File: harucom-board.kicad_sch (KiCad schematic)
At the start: 4 parts

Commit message: Rev.2 (260322)
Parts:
- H1, H2, H3, H4: footprint MountingHole:MountingHole_2.2mm_M2_ISO14580 -> MountingHole:MountingHole_2.7mm_M2.5_Pad_Via; symbol Mechanical:MountingHole -> Mechanical:MountingHole_Pad
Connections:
- new net GND: H1.1, H2.1, H3.1, H4.1
- no-connect marks 1 -> 0
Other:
- sheet Connectors ports: added I2C0_SCL, I2C0_SDA, I2C1_SCL, I2C1_SDA; removed I2C_SDA, I2C_SDL, UART1_RX, UART1_TX
- sheet USB & Power Supply ports: added LED_G, LED_R; removed LED

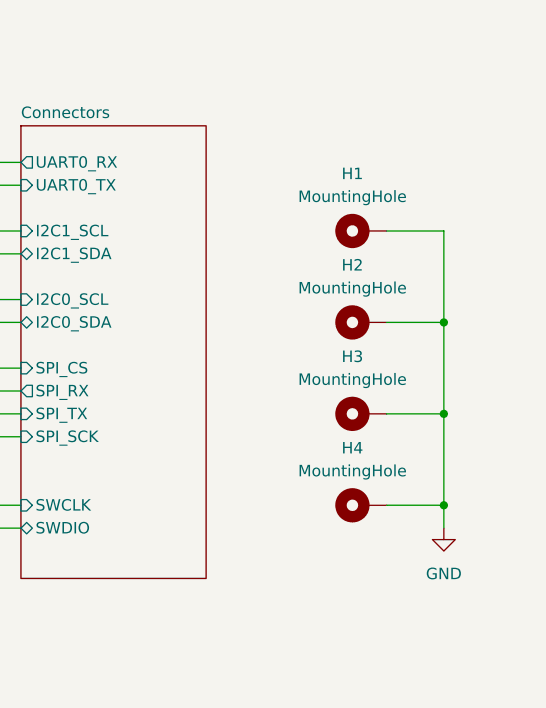
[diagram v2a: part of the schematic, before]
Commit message: Rev. 3B: Disconnect mounting holes from GND
  - Change mounting holes from MountingHole_Pad (with via) to MountingHole (ISO14580)
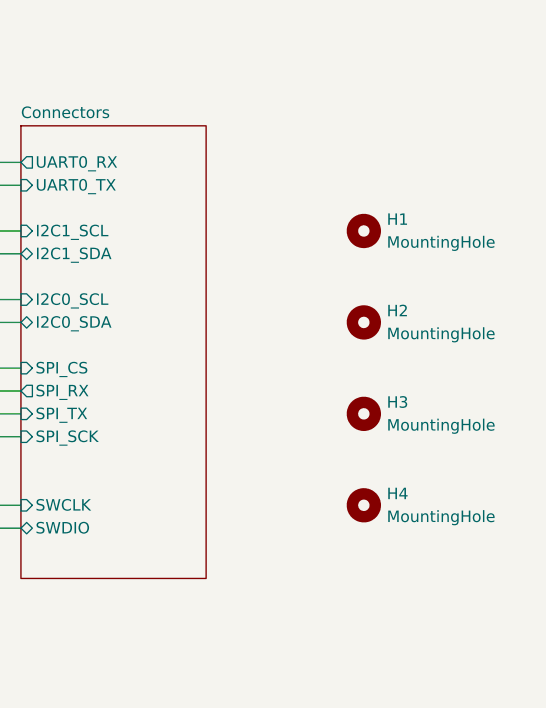
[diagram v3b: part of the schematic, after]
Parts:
- H1, H2, H3, H4: footprint MountingHole:MountingHole_2.7mm_M2.5_Pad_Via -> MountingHole:MountingHole_2.7mm_M2.5_ISO14580; symbol Mechanical:MountingHole_Pad -> Mechanical:MountingHole
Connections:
- removed net GND: H1.1, H2.1, H3.1, H4.1
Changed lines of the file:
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@@
 	(title_block
 		(title "Harucom-board")
-		(date "2026-03-23")
-		(rev "2B")
+		(date "2026-04-03")
+		(rev "3B")
 		(comment 1 "https://github.com/harukasan/harucom-board/")
 		(comment 2 "SPDX-License-Identifier: CERN-OHL-P-2.0")
@@
 		)
 	)
-	(junction
-		(at 240.03 143.51)
-		(diameter 0)
-		(color 0 0 0 0)
-	)
-	(junction
-		(at 240.03 133.35)
-		(diameter 0)
-		(color 0 0 0 0)
-	)
-	(junction
-		(at 240.03 123.19)
-		(diameter 0)
-		(color 0 0 0 0)
-	)
 	(wire
 		(pts
@@
 	(wire
 		(pts
-			(xy 240.03 143.51) (xy 240.03 133.35)
-		)
-		(stroke
-			(width 0)
-			(type default)
-		)
-	)
-	(wire
-		(pts
 			(xy 177.8 107.95) (xy 193.04 107.95)
 		)
@@
 	(wire
 		(pts
-			(xy 240.03 133.35) (xy 240.03 123.19)
-		)
-		(stroke
-			(width 0)
-			(type default)
-		)
-	)
-	(wire
-		(pts
 			(xy 78.74 63.5) (xy 91.44 63.5)
 		)
@@
 	(wire
 		(pts
-			(xy 240.03 123.19) (xy 233.68 123.19)
-		)
-		(stroke
-			(width 0)
-			(type default)
-		)
-	)
-	(wire
-		(pts
 			(xy 91.44 132.08) (xy 91.44 149.86)
 		)
@@
 	(wire
 		(pts
-			(xy 233.68 113.03) (xy 240.03 113.03)
-		)
-		(stroke
-			(width 0)
-			(type default)
-		)
-	)
-	(wire
-		(pts
-			(xy 240.03 143.51) (xy 233.68 143.51)
-		)
-		(stroke
-			(width 0)
-			(type default)
-		)
-	)
-	(wire
-		(pts
 			(xy 177.8 123.19) (xy 193.04 123.19)
 		)
@@
 	(wire
 		(pts
-			(xy 240.03 113.03) (xy 240.03 123.19)
-		)
-		(stroke
-			(width 0)
-			(type default)
-		)
-	)
-	(wire
-		(pts
 			(xy 177.8 133.35) (xy 193.04 133.35)
 		)
@@
 	(wire
 		(pts
-			(xy 240.03 133.35) (xy 233.68 133.35)
-		)
-		(stroke
-			(width 0)
-			(type default)
-		)
-	)
-	(wire
-		(pts
 			(xy 121.92 66.04) (xy 104.14 66.04)
 		)
@@
 	(wire
 		(pts
-			(xy 240.03 146.05) (xy 240.03 143.51)
-		)
-		(stroke
-			(width 0)
-			(type default)
-		)
-	)
-	(wire
-		(pts
 			(xy 53.34 87.63) (xy 71.12 87.63)
 		)
@@
 	)
 	(symbol
-		(lib_id "Mechanical:MountingHole_Pad")
+		(lib_id "Mechanical:MountingHole")
 		(at 231.14 133.35 90)
 		(unit 1)
@@
 		(fields_autoplaced yes)
 		(property "Reference" "H3"
-			(at 229.87 127 90)
+			(at 233.68 132.0799 90)
 			(effects
 				(font
 					(size 1.27 1.27)
 				)
+				(justify right)
 			)
 		)
 		(property "Value" "MountingHole"
-			(at 229.87 129.54 90)
+			(at 233.68 134.6199 90)
 			(effects
 				(font
 					(size 1.27 1.27)
 				)
+				(justify right)
 			)
 		)
-		(property "Footprint" "MountingHole:MountingHole_2.7mm_M2.5_Pad_Via"
+		(property "Footprint" "MountingHole:MountingHole_2.7mm_M2.5_ISO14580"
 			(at 231.14 133.35 0)
 			(effects
@@
 			)
 		)
-		(property "Description" "Mounting Hole with connection"
+		(property "Description" "Mounting Hole without connection"
 			(at 231.14 133.35 0)
 			(effects
@@
 			)
 		)
-		(pin "1"
-		)
 		(instances
-			(project ""
+			(project "harucom-board"
 				(path "/0cb5192e-ac62-478f-bacb-beb1b9be1a5b"
 					(reference "H3")
@@
 	)
 	(symbol
-		(lib_id "Mechanical:MountingHole_Pad")
+		(lib_id "Mechanical:MountingHole")
 		(at 231.14 123.19 90)
 		(unit 1)
@@
 		(fields_autoplaced yes)
 		(property "Reference" "H2"
-			(at 229.87 116.84 90)
+			(at 233.68 121.9199 90)
 			(effects
 				(font
 					(size 1.27 1.27)
 				)
+				(justify right)
 			)
 		)
 		(property "Value" "MountingHole"
-			(at 229.87 119.38 90)
+			(at 233.68 124.4599 90)
 			(effects
 				(font
 					(size 1.27 1.27)
 				)
+				(justify right)
 			)
 		)
-		(property "Footprint" "MountingHole:MountingHole_2.7mm_M2.5_Pad_Via"
+		(property "Footprint" "MountingHole:MountingHole_2.7mm_M2.5_ISO14580"
 			(at 231.14 123.19 0)
 			(effects
@@
 			)
 		)
-		(property "Description" "Mounting Hole with connection"
+		(property "Description" "Mounting Hole without connection"
 			(at 231.14 123.19 0)
 			(effects
@@
 			)
 		)
-		(pin "1"
-		)
 		(instances
-			(project ""
+			(project "harucom-board"
 				(path "/0cb5192e-ac62-478f-bacb-beb1b9be1a5b"
 					(reference "H2")
@@
 	)
 	(symbol
-		(lib_id "Mechanical:MountingHole_Pad")
+		(lib_id "Mechanical:MountingHole")
 		(at 231.14 113.03 90)
 		(unit 1)
@@
 		(fields_autoplaced yes)
 		(property "Reference" "H1"
-			(at 229.87 106.68 90)
+			(at 233.68 111.7599 90)
 			(effects
 				(font
 					(size 1.27 1.27)
 				)
+				(justify right)
 			)
 		)
 		(property "Value" "MountingHole"
-			(at 229.87 109.22 90)
+			(at 233.68 114.2999 90)
 			(effects
 				(font
 					(size 1.27 1.27)
 				)
+				(justify right)
 			)
 		)
-		(property "Footprint" "MountingHole:MountingHole_2.7mm_M2.5_Pad_Via"
+		(property "Footprint" "MountingHole:MountingHole_2.7mm_M2.5_ISO14580"
 			(at 231.14 113.03 0)
 			(effects
@@
 			)
 		)
-		(property "Description" "Mounting Hole with connection"
+		(property "Description" "Mounting Hole without connection"
 			(at 231.14 113.03 0)
 			(effects
@@
 			)
 		)
-		(pin "1"
-		)
 		(instances
-			(project ""
+			(project "harucom-board"
 				(path "/0cb5192e-ac62-478f-bacb-beb1b9be1a5b"
 					(reference "H1")
@@
 	)
 	(symbol
-		(lib_id "Mechanical:MountingHole_Pad")
+		(lib_id "Mechanical:MountingHole")
 		(at 231.14 143.51 90)
 		(unit 1)
@@
 		(fields_autoplaced yes)
 		(property "Reference" "H4"
-			(at 229.87 137.16 90)
+			(at 233.68 142.2399 90)
 			(effects
 				(font
 					(size 1.27 1.27)
 				)
+				(justify right)
 			)
 		)
 		(property "Value" "MountingHole"
-			(at 229.87 139.7 90)
+			(at 233.68 144.7799 90)
 			(effects
 				(font
 					(size 1.27 1.27)
 				)
+				(justify right)
 			)
 		)
-		(property "Footprint" "MountingHole:MountingHole_2.7mm_M2.5_Pad_Via"
+		(property "Footprint" "MountingHole:MountingHole_2.7mm_M2.5_ISO14580"
 			(at 231.14 143.51 0)
 			(effects
@@
 			)
 		)
-		(property "Description" "Mounting Hole with connection"
+		(property "Description" "Mounting Hole without connection"
 			(at 231.14 143.51 0)
 			(effects
@@
 			)
 		)
-		(pin "1"
-		)
 		(instances
-			(project ""
+			(project "harucom-board"
 				(path "/0cb5192e-ac62-478f-bacb-beb1b9be1a5b"
 					(reference "H4")
 					(unit 1)
 				)
-			)
-		)
-	)
-	(symbol
-		(lib_id "power:GND")
-		(at 240.03 146.05 0)
-		(unit 1)
-		(exclude_from_sim no)
-		(in_bom yes)
-		(on_board yes)
-		(dnp no)
-		(fields_autoplaced yes)
-		(property "Reference" "#PWR01"
-			(at 240.03 152.4 0)
-			(effects
-				(font
-					(size 1.27 1.27)
-				)
-				(hide yes)
-			)
-		)
-		(property "Value" "GND"
-			(at 240.03 151.13 0)
-			(effects
-				(font
-					(size 1.27 1.27)
-				)
-			)
-		)
-		(property "Footprint" ""
-			(at 240.03 146.05 0)
-			(effects
-				(font
-					(size 1.27 1.27)
-				)
-				(hide yes)
-			)
-		)
-		(property "Datasheet" ""
-			(at 240.03 146.05 0)
-			(effects
-				(font
-					(size 1.27 1.27)
-				)
-				(hide yes)
-			)
-		)
-		(property "Description" "Power symbol creates a global label with name \"GND\" , ground"
-			(at 240.03 146.05 0)
-			(effects
-				(font
-					(size 1.27 1.27)
-				)
-				(hide yes)
-			)
-		)
-		(pin "1"
-		)
-		(instances
-			(project ""
-				(path "/0cb5192e-ac62-478f-bacb-beb1b9be1a5b"
-					(reference "#PWR01")
-					(unit 1)
-				)
